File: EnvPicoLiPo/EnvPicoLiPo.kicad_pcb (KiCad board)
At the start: 2 copper layers, 21.2 x 51.6 mm, 53 parts, among them J1 SKRKAEE020, J2 2.54mm header 01x20, J3 2.54mm header 01x20, J4 Conn_01x03_Male, U1 BQ24072RGT, U2 LM3671MF 3.3, U3 RP2040, Y1 Crystal_GND24 12MHz

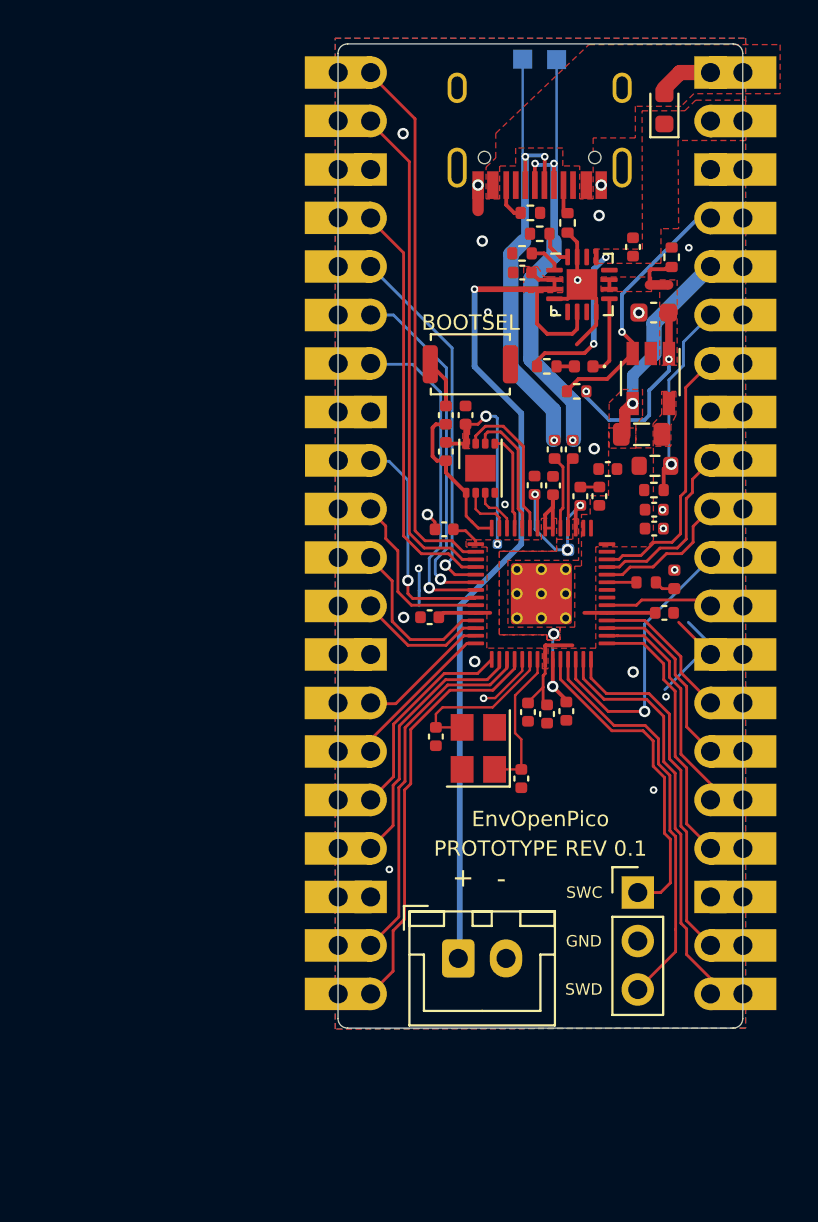
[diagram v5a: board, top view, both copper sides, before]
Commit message: overhauled battery version, not many changes other than increasing clearance across the board
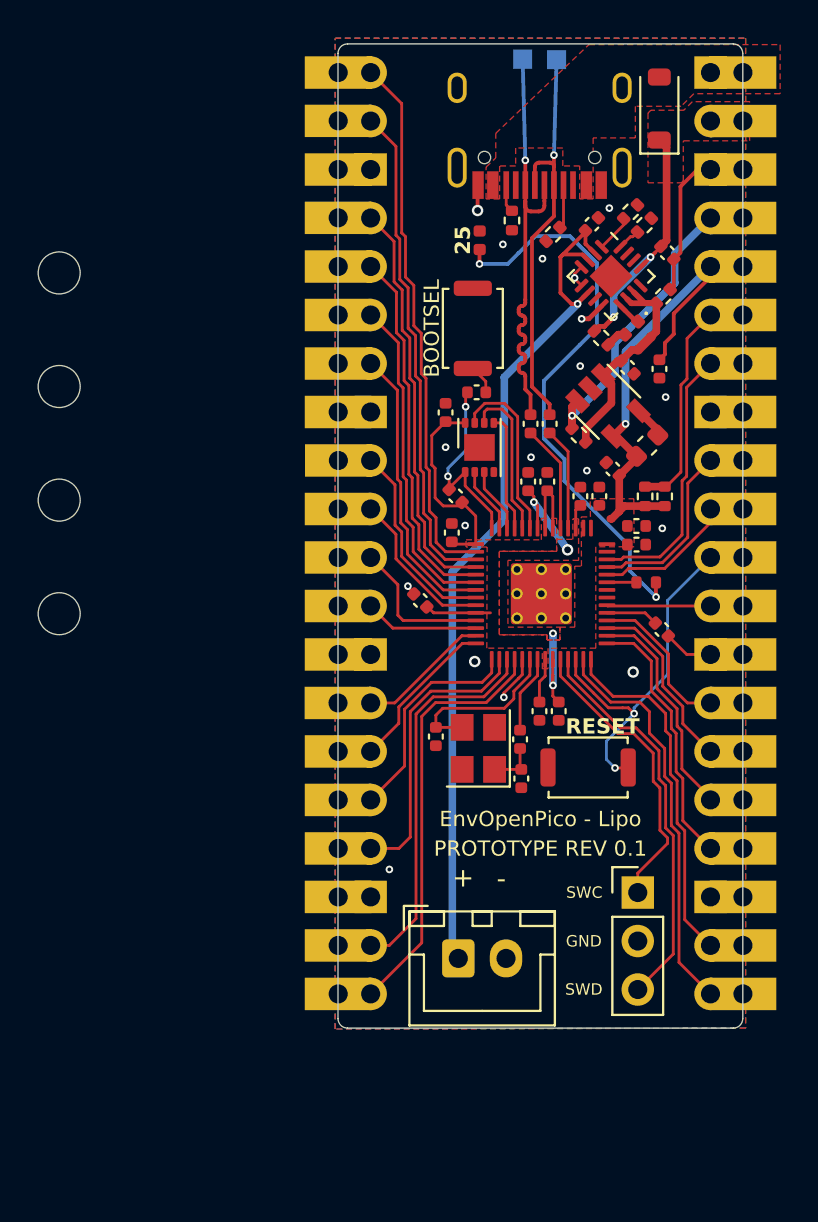
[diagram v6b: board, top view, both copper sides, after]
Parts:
- removed TP6, TP8: TestPoint, TestPoint:TestPoint_Pad_D1.0mm
- added H1: MountingHole, MountingHole:MountingHole_2.2mm_M2, F.Cu at (78.4, 69.2)
- added H2: MountingHole, MountingHole:MountingHole_2.2mm_M2, F.Cu at (78.4, 75.2)
- added H3: MountingHole, MountingHole:MountingHole_2.2mm_M2, F.Cu at (78.4, 81.1)
- added H4: MountingHole, MountingHole:MountingHole_2.2mm_M2, F.Cu at (78.4, 87.1)
- added J5: SKRKAEE020, Button_Switch_SMD:SW_Push_SPST_NO_Alps_SKRK, F.Cu at (106.1, 95.1)
- added R14: 1K 0402, Capacitor_SMD:C_0402_1005Metric, F.Cu at (102.6, 93.7)
- C3: value 10uf 0603 6.3V -> 10uf 0402 6.3V; footprint Capacitor_SMD:C_0603_1608Metric -> Capacitor_SMD:C_0402_1005Metric
- D1: value 1n4002 0603 -> 1n4002W; footprint Diode_SMD:D_0603_1608Metric -> Diode_SMD:D_SOD-123
- L1: value INDUCTOR 2.2uH 0805 -> inductor 2.2uh 600mA 0603; footprint Inductor_SMD:L_0805_2012Metric -> Inductor_SMD:L_0603_1608Metric
- R5: value 200ohm 0603 -> 200ohm 0402; footprint Resistor_SMD:R_0603_1608Metric -> Resistor_SMD:R_0402_1005Metric
- moved D3 20.5 mm to (100.5, 67.5)
- moved C20 17.7 mm to (109.9, 74.2), turned to -90 degrees
- moved C12 8.13 mm to (97.3, 86.4), turned to 135 degrees
- moved R2 6.09 mm to (108.4, 66.0), turned to -135 degrees
- moved R7 5.50 mm to (109.1, 66.7), turned to 45 degrees
- moved C4 4.44 mm to (106.3, 66.7), turned to -135 degrees
- moved R6 3.22 mm to (106.8, 72.6), turned to -45 degrees
- moved D2 3.21 mm to (108.4, 72.1), turned to -135 degrees
- moved C3 3.18 mm to (108.2, 74.2), turned to -45 degrees
- moved NT1 3.14 mm to (109.1, 72.9), turned to -135 degrees
- moved U2 2.66 mm to (107.2, 76.2), turned to -45 degrees
- moved R11 2.38 mm to (99.2, 80.9), turned to 135 degrees
- moved R4 2.30 mm to (105.7, 77.7), turned to 135 degrees
- moved C2 2.10 mm to (110.1, 70.4), turned to -135 degrees
- moved R12 2.01 mm to (100.3, 75.5), turned to 0 degrees
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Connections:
- C19 pad 2: /XOUT -> Net-(C19-Pad2)
- FLASH1 pad 9: unconnected-(FLASH1-Pad9) -> GND
- Y1 pad 1: /XOUT -> Net-(C19-Pad2)
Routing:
- net Net-(D3-A): track 1.10 -> 29.9 mm, vias 0 -> 2
- net +3V3: track 40.2 -> 48.4 mm, vias 3 -> 1
- net GND: track 23.4 -> 17.2 mm, vias 24 -> 18
- net VSYS: track 8.44 -> 13.4 mm
- net /RUN: track 14.8 -> 18.9 mm, vias 1 -> 2
- net /XOUT: track 7.78 -> 4.09 mm
- net VDD: track 9.98 -> 6.59 mm, vias 2 -> 0
- net USB_D-: track 24.7 -> 21.6 mm, vias 3 -> 1
- net Net-(D2-K): track 4.23 -> 1.27 mm
- net VBUS: track 2.78 -> 0.00 mm
- net Net-(C2-Pad2): track 2.26 -> 4.88 mm
- net +1V1: track 14.8 -> 12.2 mm, vias 5 -> 4
- net Net-(C19-Pad2): track 0.00 -> 2.52 mm
- net USB_D+: track 25.2 -> 22.8 mm, vias 3 -> 1
- net /QSPI_SS: track 8.00 -> 10.3 mm, vias 0 -> 2
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- removed copper zone on F.Cu, net Net-(C2-Pad2)
- removed copper zone on F.Cu, net Net-(U2-SW)
- removed copper zone on F.Cu, net VBAT
- removed copper zone on F.Cu, net VDD
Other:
- board text added: "25"
- board text added: "EnvOpenPico - Lipo"
- board text added: "RESET"
- board text added: "env"
- board text removed: "1.1V"
- board text removed: "3.3V"
- board text removed: "DNF"
- board text removed: "EnvOpenPico"
